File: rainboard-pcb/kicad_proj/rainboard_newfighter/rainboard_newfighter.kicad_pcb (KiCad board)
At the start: 4 copper layers, 260 x 253.6 mm, 420 parts, among them J1 54-00167, J10 Conn_01x02_Female, J11 Conn_01x02_Female, J12 Conn_01x02_Female, J13 Conn_01x02_Female, J14 Conn_01x02_Female, J15 SDS-50J, J16 Conn_01x02_Female, J17 PH2-06-UA, J18 Conn_01x03, J19 Conn_01x03, J20 PH2-06-UA, J21 PH2-06-UA, J3 USB_B, J4 Conn_01x02_Female, J5 Conn_01x02_Female, J6 Conn_01x02_Female, J7 Conn_01x02_Female, J8 Conn_01x02_Female, J9 Conn_01x02_Female, Q2 DUAL 30V NMOS, Q3 DUAL 30V NMOS, SW1 SANWA-OBSF24, SW10 SANWA-OBSF24, SW11 SANWA-OBSF24, SW12 SANWA-OBSF24, SW13 SANWA-OBSF24, SW14 SANWA-OBSF24, SW15 SANWA-OBSF24, SW16 SANWA-OBSF24, SW17 SANWA-OBSF24, SW18 SANWA-OBSF24, SW19 SANWA-OBSF24, SW2 SANWA-OBSF24, SW20 SANWA-OBSF24, SW21 SANWA-OBSF24, SW22 SANWA-OBSF24, SW23 SANWA-OBSF24, SW24 SANWA-OBSF24, SW25 SANWA-OBSF24, SW26 SANWA-OBSF24, SW27 SANWA-OBSF24, SW28 SANWA-OBSF24, SW29 SANWA-OBSF24, SW3 SANWA-OBSF24, SW30 SANWA-OBSF24, SW31 SANWA-OBSF24, SW32 SANWA-OBSF24, SW33 SANWA-OBSF24, SW34 SANWA-OBSF24, SW35 SANWA-OBSF24, SW36 SANWA-OBSF24, SW37 SANWA-OBSF24, SW38 SANWA-OBSF24, SW39 SANWA-OBSF24, SW4 SANWA-OBSF24, SW40 SANWA-OBSF24, SW41 SANWA-OBSF24, SW42 SANWA-OBSF24, SW43 SANWA-OBSF24, SW44 SANWA-OBSF24, SW45 SANWA-OBSF24, SW46 SANWA-OBSF24, SW47 SANWA-OBSF24, SW48 SANWA-OBSF24, SW49 SANWA-OBSF24, SW5 SANWA-OBSF24, SW50 SANWA-OBSF24, SW51 SANWA-OBSF24, SW52 SANWA-OBSF24, SW53 SANWA-OBSF24, SW54 SANWA-OBSF24, SW55 SANWA-OBSF24, SW56 SANWA-OBSF24, SW57 SANWA-OBSF24, SW58 SANWA-OBSF24, SW59 SANWA-OBSF24, SW6 SANWA-OBSF24, SW60 SANWA-OBSF24, SW61 SANWA-OBSF24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

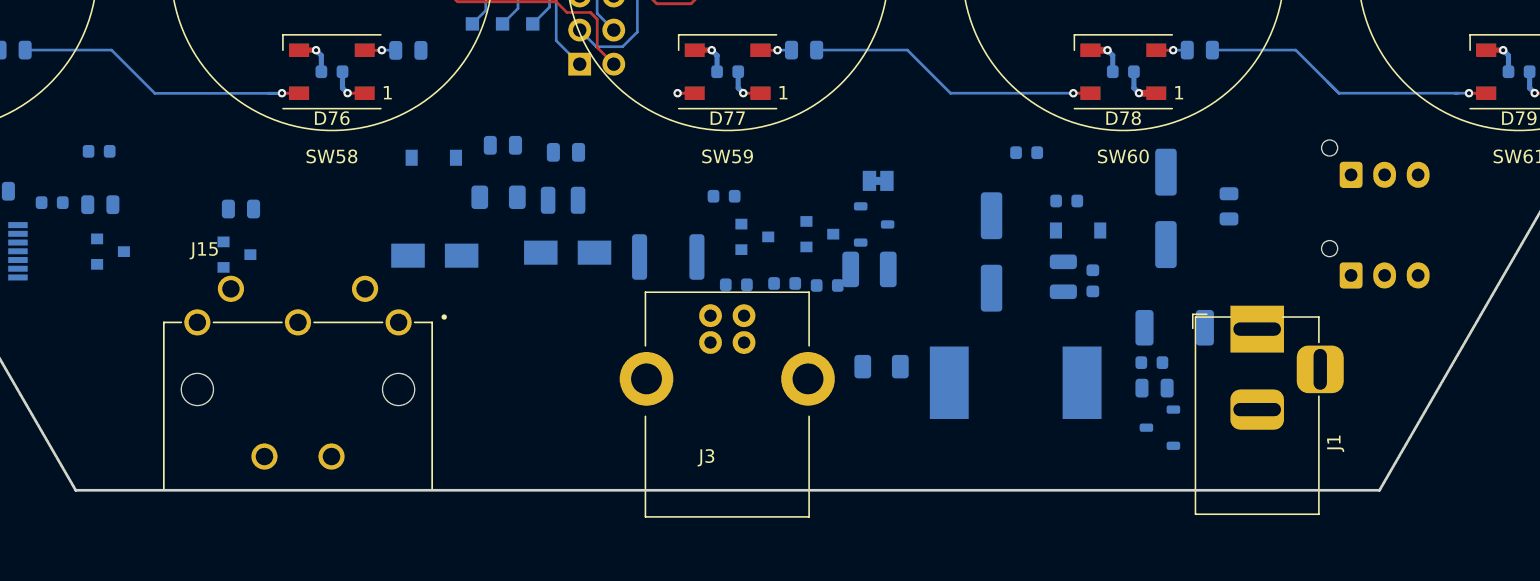
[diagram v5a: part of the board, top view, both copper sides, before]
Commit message: position the interfaces, first pass
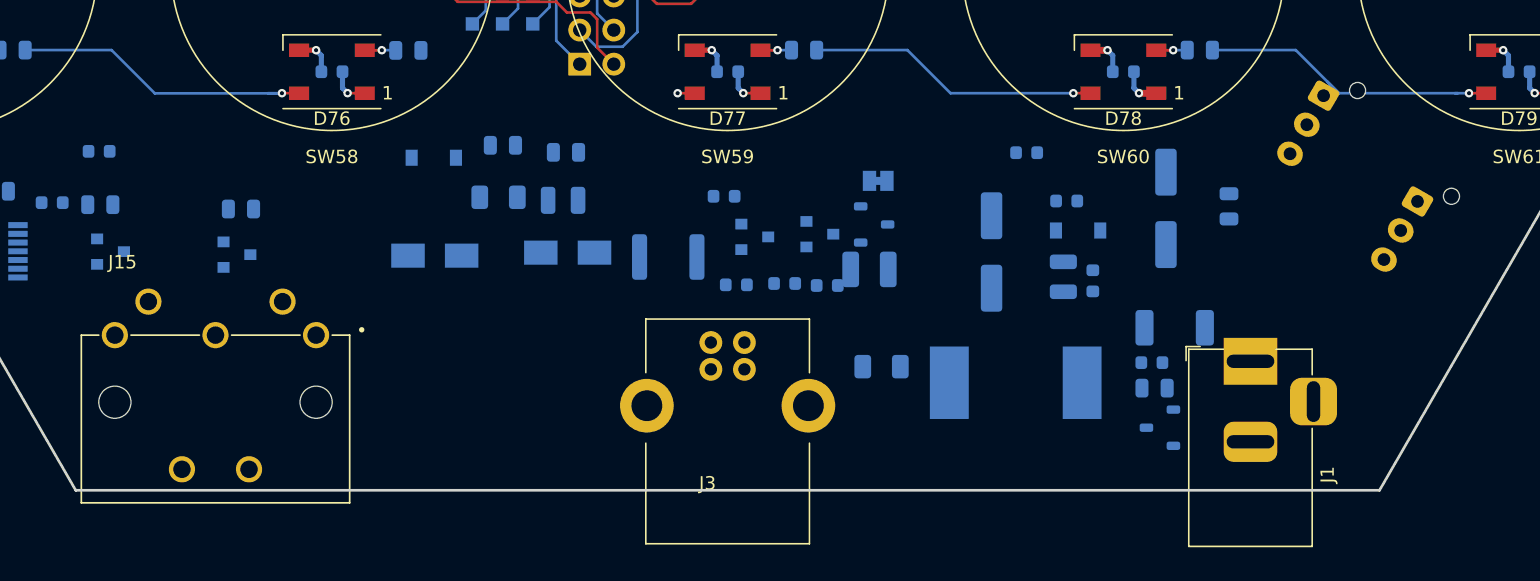
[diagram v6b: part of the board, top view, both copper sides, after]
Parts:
- moved J18 7.41 mm to (51.4, 119.5), turned to 240 degrees
- moved J19 6.25 mm to (44.4, 111.6), turned to 240 degrees
- moved J15 6.22 mm to (-38.2, 129.4)
- moved J1 2.45 mm to (39.0, 131.4)
- moved J3 2.00 mm to (0.00, 131.0)
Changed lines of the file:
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@@
-(kicad_pcb (version 20171130) (host pcbnew "(5.1.5)-3")
+(kicad_pcb (version 20171130) (host pcbnew "(5.1.5-0-10_14)")
   (general
     (thickness 1.6)
-    (drawings 6)
+    (drawings 8)
     (tracks 2423)
     (zones 0)
@@
   )
   (module rainboard_fp:BarrelJack_Horizontal (layer F.Cu)
-    (at 39.4735 128.9845 90)
+    (at 38.9735 131.3845 90)
     (descr "DC Barrel Jack")
     (tags "Power Jack")
@@
   )
   (module Connector_JST:JST_XH_B3B-XH-AM_1x03_P2.50mm_Vertical (layer B.Cu)
-    (at 46.4735 117.4845)
+    (at 44.4235 111.5845 240)
     (descr "JST XH series connector, B3B-XH-AM, with boss (http://www.jst-mfg.com/product/pdf/eng/eXH.pdf), generated with kicad-footprint-generator")
     (tags "connector JST XH vertical boss")
-    (fp_text reference J19 (at -4.5 -3.5) (layer B.SilkS)
+    (fp_text reference J19 (at -4.5 -3.5 60) (layer B.SilkS)
       (effects (font (size 1 1) (thickness 0.15)) (justify mirror))
     )
-    (fp_text value Conn_01x03 (at 2.5 -4.6) (layer B.Fab)
+    (fp_text value Conn_01x03 (at 2.5 -4.6 60) (layer B.Fab)
       (effects (font (size 1 1) (thickness 0.15)) (justify mirror))
     )
@@
     (fp_line (start -2.45 -3.4) (end 7.45 -3.4) (layer B.Fab) (width 0.1))
     (fp_line (start -2.45 2.35) (end -2.45 -3.4) (layer B.Fab) (width 0.1))
-    (fp_text user %R (at 2.5 -2.7) (layer B.Fab)
+    (fp_text user %R (at 2.5 -2.7 60) (layer B.Fab)
       (effects (font (size 1 1) (thickness 0.15)) (justify mirror))
     )
-    (pad 1 thru_hole roundrect (at 0 0) (size 1.7 1.95) (drill 0.95) (layers *.Cu *.Mask) (roundrect_rratio 0.147059)
+    (pad 1 thru_hole roundrect (at 0 0 240) (size 1.7 1.95) (drill 0.95) (layers *.Cu *.Mask) (roundrect_rratio 0.147059)
       (net 4 AREF))
-    (pad 2 thru_hole oval (at 2.5 0) (size 1.7 1.95) (drill 0.95) (layers *.Cu *.Mask)
+    (pad 2 thru_hole oval (at 2.5 0 240) (size 1.7 1.95) (drill 0.95) (layers *.Cu *.Mask)
       (net 2 softpot-2))
-    (pad 3 thru_hole oval (at 5 0) (size 1.7 1.95) (drill 0.95) (layers *.Cu *.Mask)
+    (pad 3 thru_hole oval (at 5 0 240) (size 1.7 1.95) (drill 0.95) (layers *.Cu *.Mask)
       (net 5 BREF))
-    (pad "" np_thru_hole circle (at -1.6 -2) (size 1.2 1.2) (drill 1.2) (layers *.Cu *.Mask))
+    (pad "" np_thru_hole circle (at -1.6 -2 240) (size 1.2 1.2) (drill 1.2) (layers *.Cu *.Mask))
     (model ${KISYS3DMOD}/Connector_JST.3dshapes/JST_XH_B3B-XH-AM_1x03_P2.50mm_Vertical.wrl
       (at (xyz 0 0 0))
@@
   )
   (module Connector_JST:JST_XH_B3B-XH-AM_1x03_P2.50mm_Vertical (layer B.Cu)
-    (at 46.4735 124.9845)
+    (at 51.4235 119.469436 240)
     (descr "JST XH series connector, B3B-XH-AM, with boss (http://www.jst-mfg.com/product/pdf/eng/eXH.pdf), generated with kicad-footprint-generator")
     (tags "connector JST XH vertical boss")
-    (fp_text reference J18 (at 2.5 3.55) (layer B.SilkS)
+    (fp_text reference J18 (at 2.5 3.55 60) (layer B.SilkS)
       (effects (font (size 1 1) (thickness 0.15)) (justify mirror))
     )
-    (fp_text value Conn_01x03 (at 2.5 -4.6) (layer B.Fab)
+    (fp_text value Conn_01x03 (at 2.5 -4.6 60) (layer B.Fab)
       (effects (font (size 1 1) (thickness 0.15)) (justify mirror))
     )
@@
     (fp_line (start -2.45 -3.4) (end 7.45 -3.4) (layer B.Fab) (width 0.1))
     (fp_line (start -2.45 2.35) (end -2.45 -3.4) (layer B.Fab) (width 0.1))
-    (fp_text user %R (at 2.5 -2.7) (layer B.Fab)
+    (fp_text user %R (at 2.5 -2.7 60) (layer B.Fab)
       (effects (font (size 1 1) (thickness 0.15)) (justify mirror))
     )
-    (pad 1 thru_hole roundrect (at 0 0) (size 1.7 1.95) (drill 0.95) (layers *.Cu *.Mask) (roundrect_rratio 0.147059)
+    (pad 1 thru_hole roundrect (at 0 0 240) (size 1.7 1.95) (drill 0.95) (layers *.Cu *.Mask) (roundrect_rratio 0.147059)
       (net 4 AREF))
-    (pad 2 thru_hole oval (at 2.5 0) (size 1.7 1.95) (drill 0.95) (layers *.Cu *.Mask)
+    (pad 2 thru_hole oval (at 2.5 0 240) (size 1.7 1.95) (drill 0.95) (layers *.Cu *.Mask)
       (net 1 softpot-1))
-    (pad 3 thru_hole oval (at 5 0) (size 1.7 1.95) (drill 0.95) (layers *.Cu *.Mask)
+    (pad 3 thru_hole oval (at 5 0 240) (size 1.7 1.95) (drill 0.95) (layers *.Cu *.Mask)
       (net 5 BREF))
-    (pad "" np_thru_hole circle (at -1.6 -2) (size 1.2 1.2) (drill 1.2) (layers *.Cu *.Mask))
+    (pad "" np_thru_hole circle (at -1.6 -2 240) (size 1.2 1.2) (drill 1.2) (layers *.Cu *.Mask))
     (model ${KISYS3DMOD}/Connector_JST.3dshapes/JST_XH_B3B-XH-AM_1x03_P2.50mm_Vertical.wrl
       (at (xyz 0 0 0))
@@
   )
   (module rainboard_fp:CUI_SDS-50J (layer F.Cu)
-    (at -32.0265 128.4845)
+    (at -38.1765 129.4345)
     (fp_text reference J15 (at -6.929875 -5.438805) (layer F.SilkS)
       (effects (font (size 1.000701 1.000701) (thickness 0.015)))
@@
   )
   (module rainboard_fp:UJ2-BH-1-TH (layer F.Cu)
-    (at -0.0265 128.9845)
+    (at 0 130.9845)
     (fp_text reference J3 (at -1.5 9.5) (layer F.SilkS)
       (effects (font (size 1 1) (thickness 0.15)))
@@
     )
   )
+  (dimension 4.450281 (width 0.12) (layer F.SilkS)
+    (gr_text "4.450 mm" (at -10.47142 143.245231 89.35625429) (layer F.SilkS)
+      (effects (font (size 1 1) (thickness 0.15)))
+    )
+    (feature1 (pts (xy -9.2265 145.4845) (xy -9.812884 145.477911)))
+    (feature2 (pts (xy -9.1765 141.0345) (xy -9.762884 141.027911)))
+    (crossbar (pts (xy -9.1765 141.0345) (xy -9.2265 145.4845)))
+    (arrow1a (pts (xy -9.2265 145.4845) (xy -9.800227 144.351479)))
+    (arrow1b (pts (xy -9.2265 145.4845) (xy -8.62746 144.364656)))
+    (arrow2a (pts (xy -9.1765 141.0345) (xy -9.77554 142.154344)))
+    (arrow2b (pts (xy -9.1765 141.0345) (xy -8.602773 142.167521)))
+  )
+  (dimension 4.450281 (width 0.12) (layer F.SilkS)
+    (gr_text "4.450 mm" (at 34.02858 143.145231 89.35625429) (layer F.SilkS)
+      (effects (font (size 1 1) (thickness 0.15)))
+    )
+    (feature1 (pts (xy 35.2735 145.3845) (xy 34.687116 145.377911)))
+    (feature2 (pts (xy 35.3235 140.9345) (xy 34.737116 140.927911)))
+    (crossbar (pts (xy 35.3235 140.9345) (xy 35.2735 145.3845)))
+    (arrow1a (pts (xy 35.2735 145.3845) (xy 34.699773 144.251479)))
+    (arrow1b (pts (xy 35.2735 145.3845) (xy 35.87254 144.264656)))
+    (arrow2a (pts (xy 35.3235 140.9345) (xy 34.72446 142.054344)))
+    (arrow2b (pts (xy 35.3235 140.9345) (xy 35.897227 142.067521)))
+  )
   (gr_line (start -48.5936 141) (end 48.5936 141) (layer Edge.Cuts) (width 0.2))

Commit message: routing
button array routing complete
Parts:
- moved R50 174.8 mm to (18.7, 39.3)
- moved C46 172.3 mm to (18.7, 37.7)
- moved C41 117.5 mm to (67.4, 139.7)
- moved C39 117.5 mm to (58.3, 139.9)
- moved C40 117.5 mm to (58.7, 143.1)
- moved L5 117.2 mm to (62.9, 140.6)
- moved R34 116.6 mm to (-59.2, 26.5), turned to 90 degrees
- moved Q2 116.3 mm to (-56.8, 26.5), turned to 270 degrees
- moved R33 115.3 mm to (-54.2, 26.5), turned to 270 degrees
- moved TP26 114.1 mm to (-52.4, 34.8), turned to 270 degrees
- moved D15 113.9 mm to (38.2, 111.4), turned to 180 degrees
- moved D14 112.6 mm to (39.4, 124.7), turned to 180 degrees
- moved Y2 112.1 mm to (-59.2, 30.8)
- moved C42 111.4 mm to (61.0, 132.4)
- moved TP21 108.0 mm to (-51.4, 42.1), turned to 270 degrees
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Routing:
- net BTN30: track 0.00 -> 202.9 mm, vias 0 -> 2
- net BTN23: track 0.00 -> 201.6 mm, vias 0 -> 2
- net BTN22: track 0.00 -> 194.3 mm, vias 0 -> 2
- net BTN24: track 0.00 -> 174.8 mm, vias 0 -> 2
- net BTN29: track 0.00 -> 171.3 mm, vias 0 -> 2
- net softpot-2: track 0.00 -> 157.1 mm, vias 0 -> 1
- net BTN16: track 0.00 -> 157.0 mm, vias 0 -> 1
- net BREF: track 0.00 -> 155.9 mm, vias 0 -> 1
- net BTN31: track 0.00 -> 153.9 mm, vias 0 -> 2
- net BTN10: track 13.1 -> 161.3 mm, vias 0 -> 3
- net BTN48: track 0.00 -> 147.4 mm, vias 0 -> 2
- net BTN47: track 0.00 -> 138.2 mm, vias 0 -> 2
- net softpot-1: track 0.00 -> 138.1 mm, vias 0 -> 1
- net BTN39: track 0.00 -> 137.9 mm
- net BTN40: track 0.00 -> 137.7 mm, vias 0 -> 2
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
